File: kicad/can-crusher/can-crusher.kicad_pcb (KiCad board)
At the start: 2 copper layers, 21 parts, among them J1 Stepper Right, J2 Control UART, J3 Ext power, J4 Stepper Left, J5 Barrel_Jack, J6 Expansion Port, Q1 IRF4905, Q2 BS170, SW1 Reboot, SW2 User Interaction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

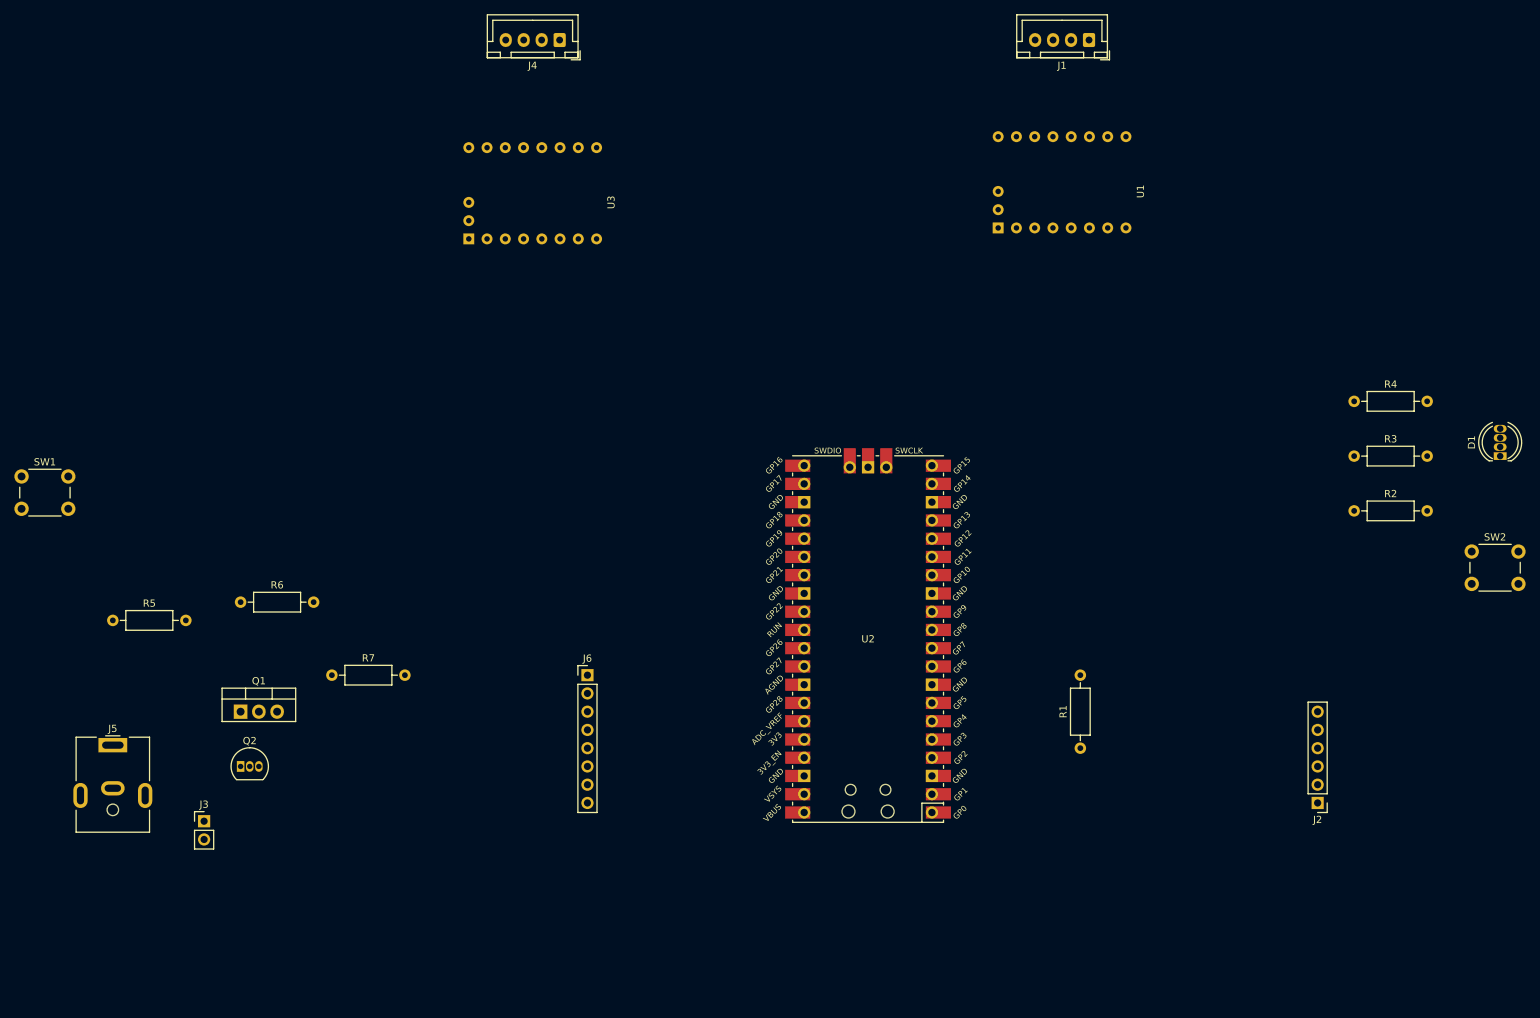
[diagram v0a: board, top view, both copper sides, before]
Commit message: Give better name to project lib storage dir
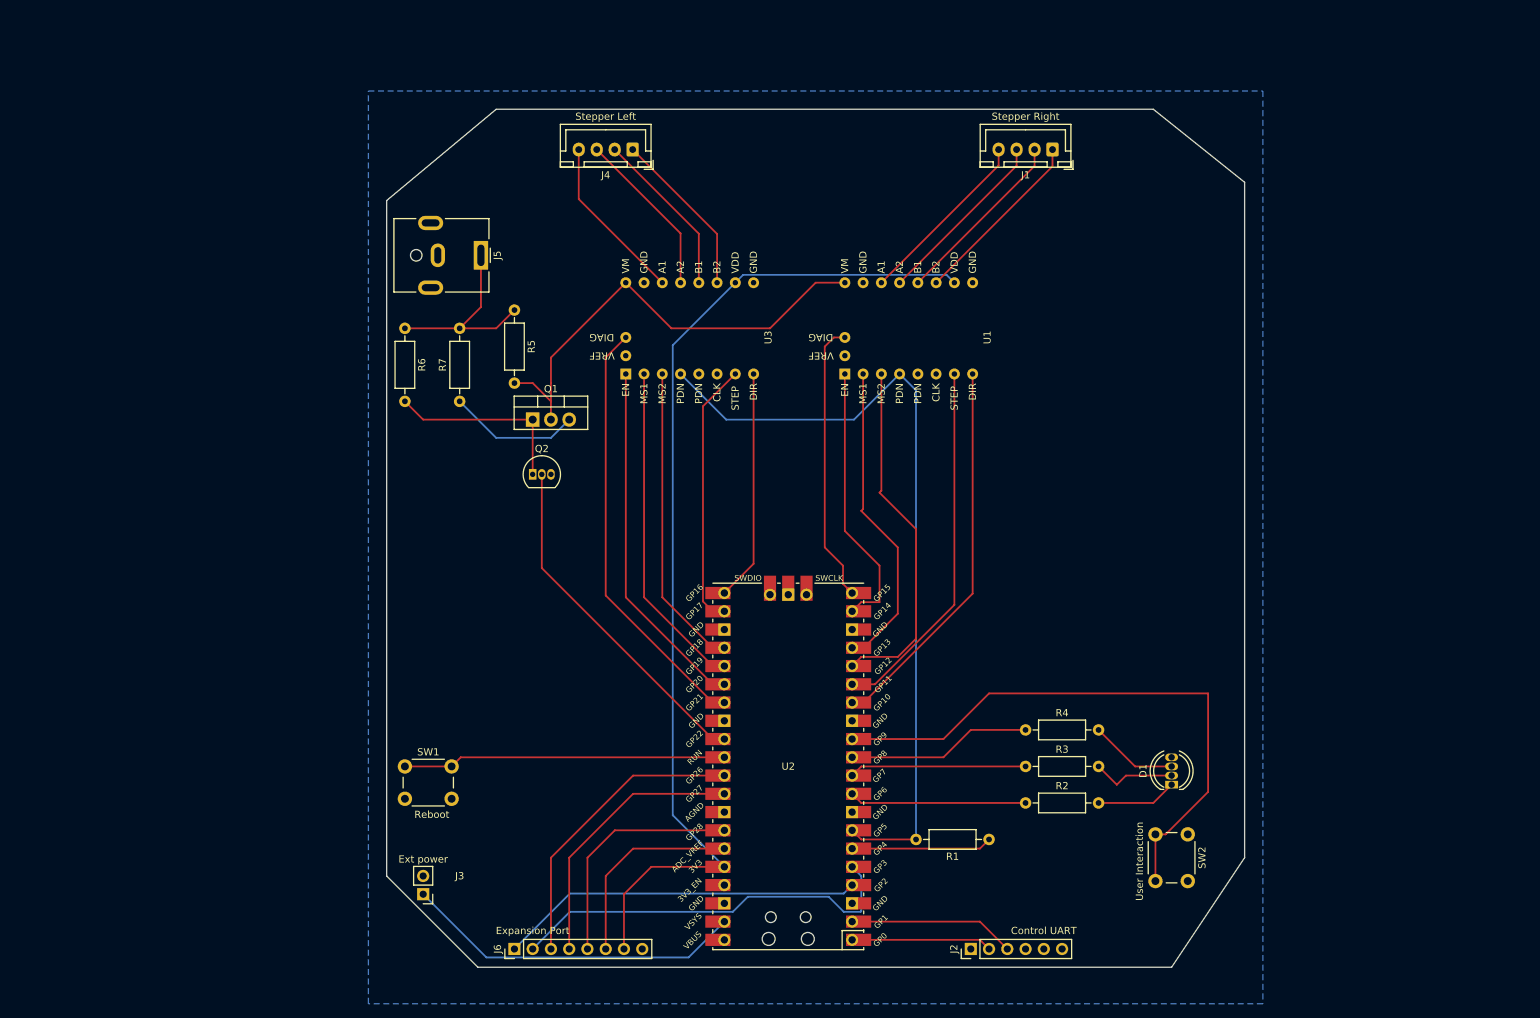
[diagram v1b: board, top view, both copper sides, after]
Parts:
- moved J5 85.3 mm to (104.6, 53.3), turned to -90 degrees
- moved R5 70.6 mm to (109.2, 61.0), turned to -90 degrees
- moved SW1 66.9 mm to (94.0, 124.5)
- moved D1 64.7 mm to (200.7, 127.0)
- moved R4 64.7 mm to (180.3, 119.4)
- moved R3 62.9 mm to (180.3, 124.5)
- moved R2 61.2 mm to (180.3, 129.5)
- moved Q1 57.5 mm to (111.8, 76.2)
- moved Q2 57.5 mm to (111.8, 83.8)
- moved SW2 55.8 mm to (202.9, 133.9), turned to -90 degrees
- moved J2 52.4 mm to (172.7, 149.9), turned to 90 degrees
- moved R6 44.4 mm to (94.0, 63.5), turned to -90 degrees
- moved R7 42.0 mm to (101.6, 73.7), turned to 90 degrees
- moved J6 39.4 mm to (109.2, 149.9), turned to 90 degrees
- moved J3 32.1 mm to (96.5, 142.2), turned to 180 degrees
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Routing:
- net +3.3V: track 0.00 -> 142.4 mm
- net /STEP_TXRX: track 0.00 -> 110.9 mm
- net Net-(SW2-Pad2): track 0.00 -> 82.1 mm
- net /12V_ON: track 0.00 -> 65.2 mm
- net Net-(U2-Pad27): track 0.00 -> 59.7 mm
- net Net-(J6-Pad2): track 0.00 -> 56.3 mm
- net Net-(U1-Pad8): track 0.00 -> 53.6 mm
- net Net-(U1-Pad7): track 0.00 -> 50.9 mm
- net Net-(J6-Pad1): track 0.00 -> 50.7 mm
- net Net-(U2-Pad26): track 0.00 -> 49.8 mm
- net Net-(U1-Pad3): track 0.00 -> 49.5 mm
- net Net-(Q2-Pad2): track 0.00 -> 48.3 mm
- net VCC: track 0.00 -> 47.6 mm
- net Net-(U2-Pad25): track 0.00 -> 46.2 mm
- net Net-(SW1-Pad1): track 0.00 -> 45.0 mm
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- added copper zone on B.Cu, net GND
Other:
- board outline added: 119.4 x 119.4 mm

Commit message: Make board more compact; make power traces appropriate sized.
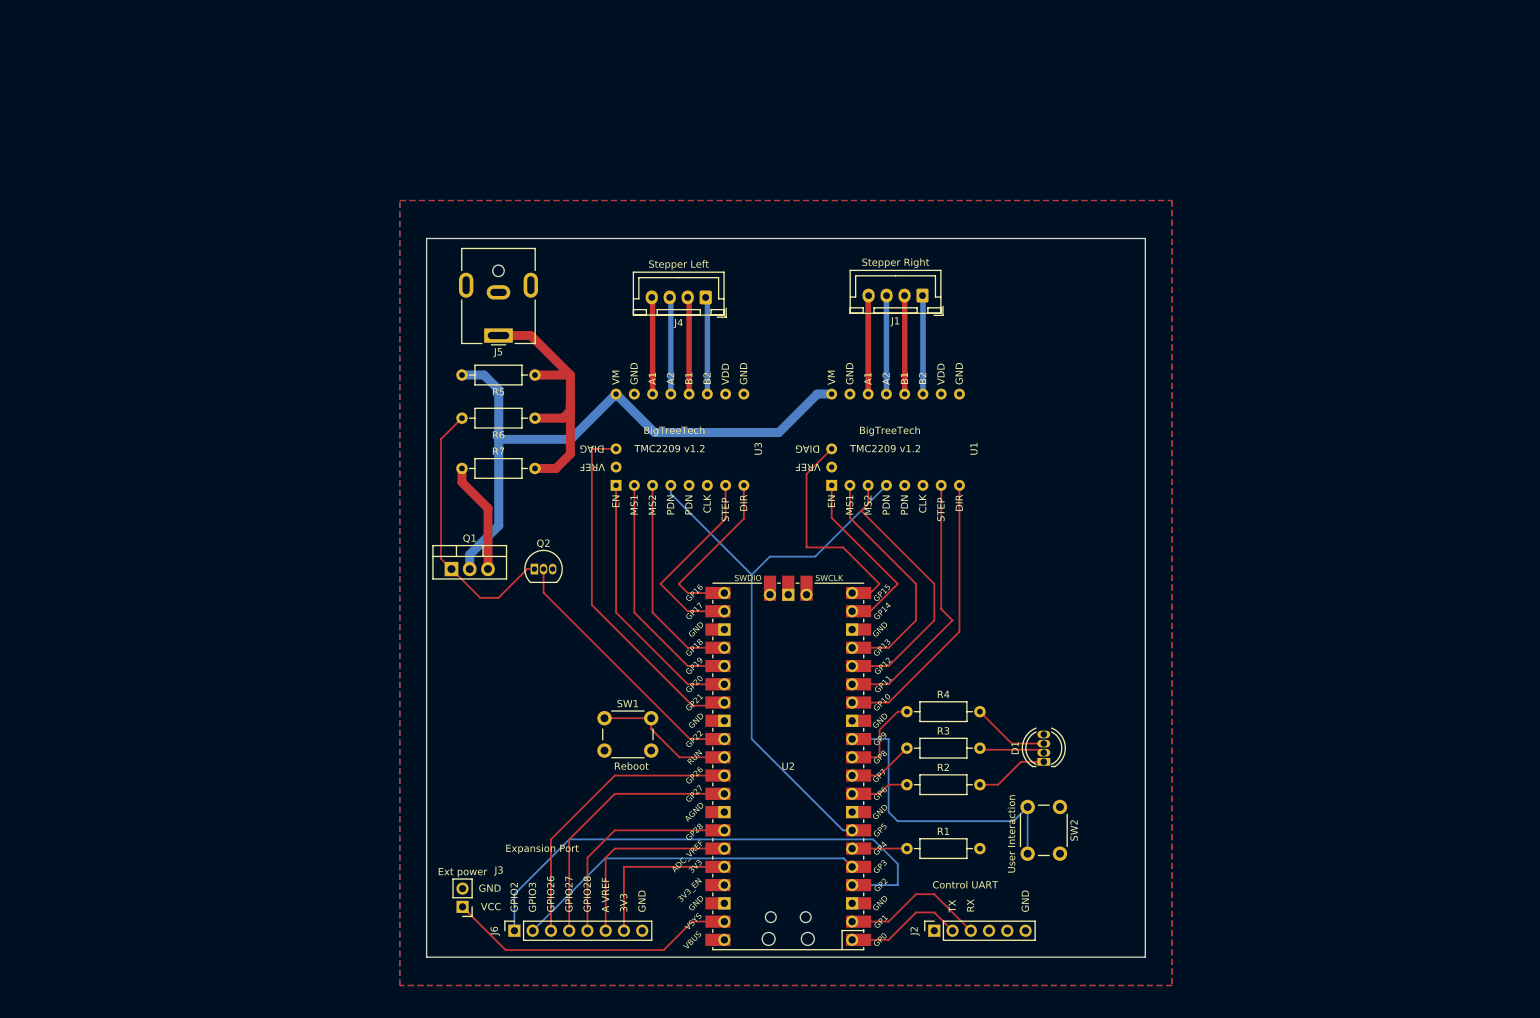
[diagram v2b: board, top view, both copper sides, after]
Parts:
- J2: footprint Connector_PinHeader_2.54mm:PinHeader_1x06_P2.54mm_Vertical -> Connector_PinSocket_2.54mm:PinSocket_1x06_P2.54mm_Vertical
- J6: footprint Connector_PinHeader_2.54mm:PinHeader_1x08_P2.54mm_Vertical -> Connector_PinSocket_2.54mm:PinSocket_1x08_P2.54mm_Vertical
- moved SW1 28.6 mm to (121.8, 117.8)
- moved J1 27.2 mm to (166.0, 58.9)
- moved Q1 23.7 mm to (100.5, 97.0)
- moved J4 22.9 mm to (135.8, 59.2)
- moved R6 22.0 mm to (112.1, 76.0), turned to 180 degrees
- moved SW2 18.2 mm to (185.1, 130.1)
- moved D1 18.1 mm to (182.9, 123.8)
- moved R2 16.7 mm to (163.8, 127.0)
- moved R3 16.7 mm to (163.8, 121.9)
- moved R4 16.7 mm to (163.8, 116.8)
- moved U1 15.6 mm to (173.7, 80.3)
- moved U3 15.6 mm to (143.7, 80.3)
- moved Q2 13.2 mm to (112.0, 97.0)
- moved R1 11.5 mm to (163.8, 135.9), turned to 0 degrees
- moved J5 11.4 mm to (107.0, 64.5), turned to 180 degrees
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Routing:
- net +3.3V: track 142.4 -> 22.9 mm
- net Net-(SW2-Pad2): track 82.1 -> 42.4 mm
- net /STEP_TXRX: track 110.9 -> 83.1 mm
- net Net-(SW1-Pad1): track 45.0 -> 19.8 mm
- net Net-(J6-Pad1): track 50.7 -> 72.3 mm
- net /12V_ON: track 65.2 -> 86.0 mm
- net Net-(R2-Pad1): track 24.7 -> 8.15 mm
- net Net-(R3-Pad1): track 24.7 -> 9.20 mm
- net Net-(U1-Pad8): track 53.6 -> 39.4 mm
- net Net-(U1-Pad7): track 50.9 -> 37.1 mm
- net Net-(R4-Pad1): track 25.7 -> 12.5 mm
- net Net-(U2-Pad26): track 49.8 -> 36.9 mm
- net Net-(U2-Pad25): track 46.2 -> 33.3 mm
- net Net-(U2-Pad24): track 42.6 -> 29.7 mm
- net Net-(U1-Pad1): track 38.1 -> 25.4 mm
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- added copper zone on F.Cu, net GND
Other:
- board size 119.4 x 119.4 mm -> 100 x 100 mm

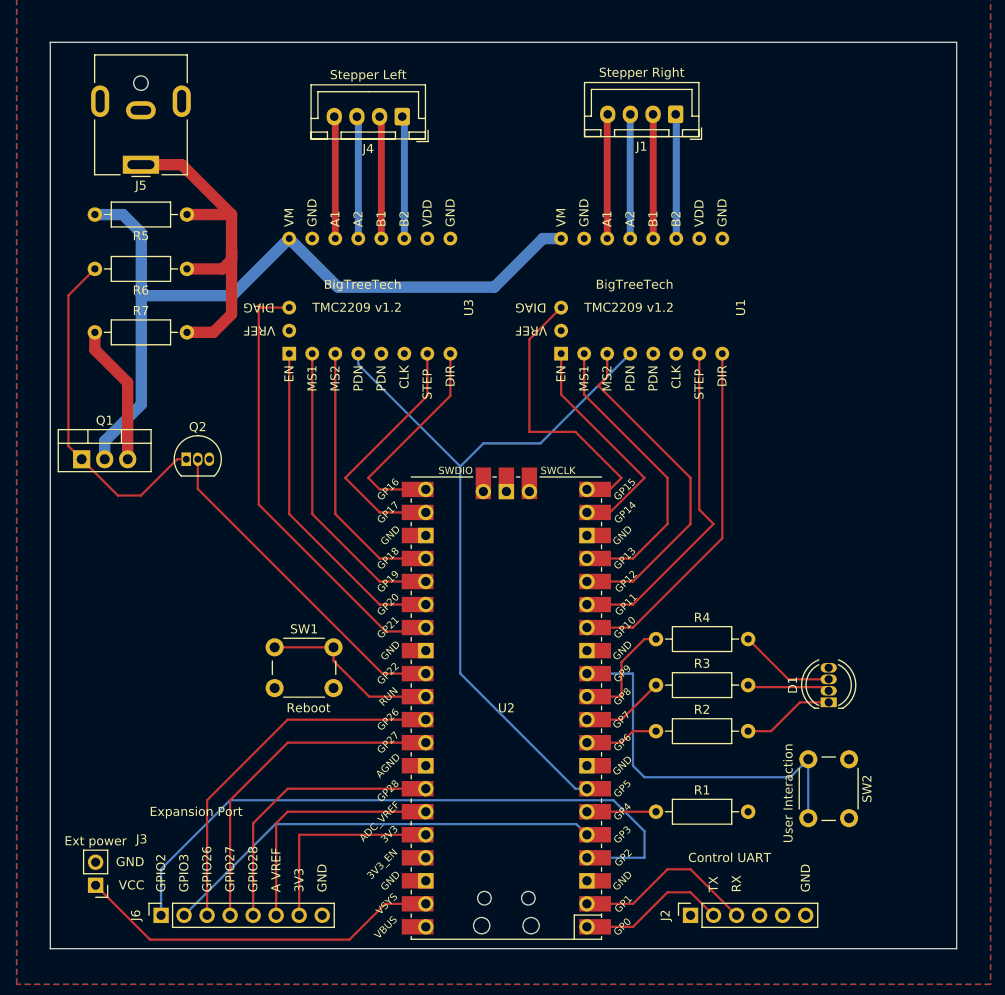
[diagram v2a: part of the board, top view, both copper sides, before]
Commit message: Final REV 1 control board submitted for PCB manufacturing
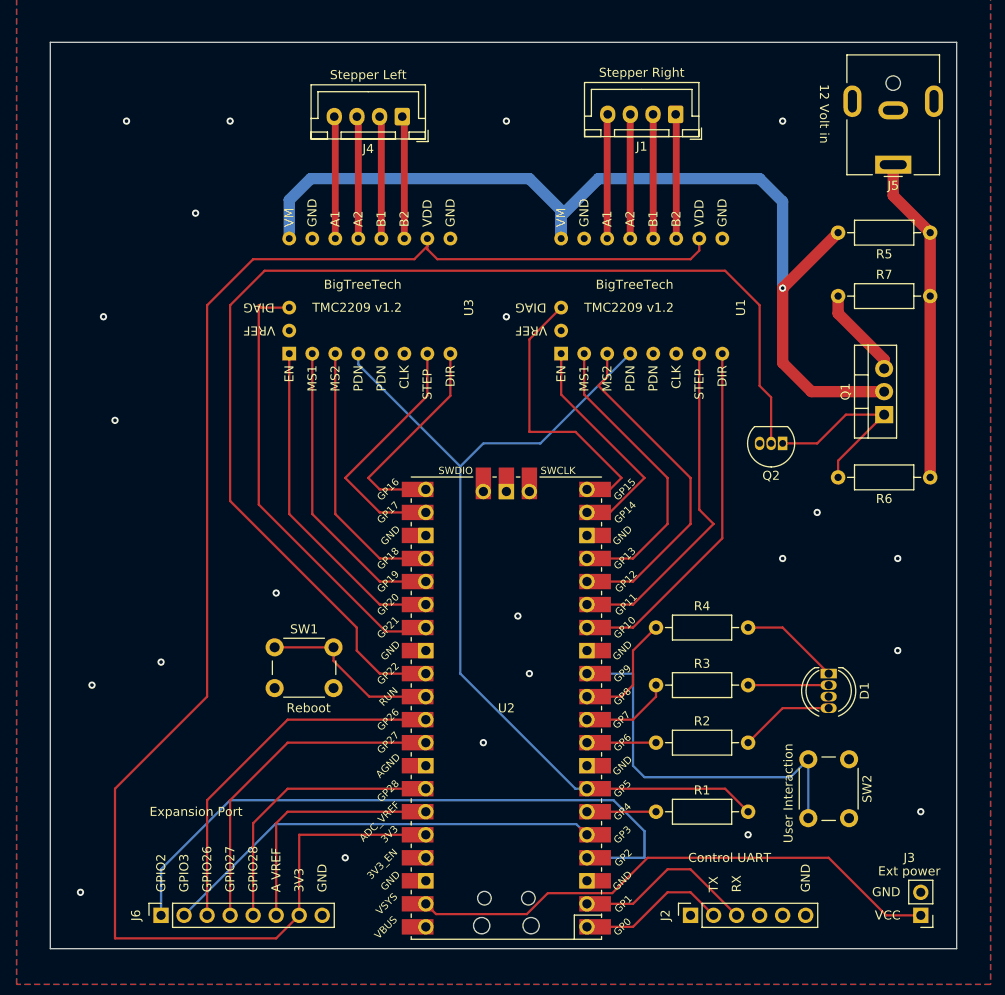
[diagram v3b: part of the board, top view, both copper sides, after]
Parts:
- D1: value LED_RGBK -> LED_BRKG
- Q1: value IRF4905 -> IRF9540N
- R2, R3, R4: value R -> 220
- moved J3 91.1 mm to (193.0, 147.3)
- moved Q1 88.7 mm to (189.0, 92.1), turned to 90 degrees
- moved R6 85.2 mm to (194.1, 99.0)
- moved J5 83.0 mm to (190.0, 64.5)
- moved R7 82.1 mm to (183.9, 79.0)
- moved R5 82.0 mm to (194.1, 72.0)
- moved Q2 65.8 mm to (177.8, 95.2), turned to 180 degrees
- moved D1 3.17 mm to (182.9, 120.7), turned to -90 degrees
- moved R2 1.27 mm to (163.8, 128.3)
- moved R4 1.27 mm to (163.8, 115.6)
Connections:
- D1 pad 3: Net-(D1-Pad3) -> GND
- D1 pad 4: GND -> Net-(D1-Pad4)
- R2 pad 2: Net-(D1-Pad1) -> Net-(D1-Pad4)
- R4 pad 2: Net-(D1-Pad3) -> Net-(D1-Pad1)
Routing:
- net +3.3V: track 22.9 -> 179.5 mm
- net Net-(Q2-Pad2): track 36.9 -> 129.9 mm
- net /12V_ON: track 86.0 -> 108.4 mm, vias 0 -> 1
- net VCC: track 40.6 -> 60.3 mm
- net /STEP_TXRX: track 83.1 -> 101.9 mm
- net Net-(Q1-Pad1): track 37.7 -> 21.5 mm
- net Net-(D1-Pad3): track 10.7 -> 0.00 mm
- net Net-(D1-Pad4): track 0.00 -> 10.5 mm
- net Net-(Q1-Pad3): track 15.5 -> 10.1 mm
- net +12V: track 40.3 -> 36.2 mm
- net Net-(D1-Pad1): track 10.2 -> 11.0 mm
- net Net-(R3-Pad1): track 9.20 -> 9.94 mm
- net Net-(R2-Pad1): track 8.15 -> 7.62 mm
- net Net-(R4-Pad1): track 12.5 -> 13.0 mm
- net GND: vias 0 -> 22
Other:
- board text added: "${COMPANY}"
- board text added: "${ISSUE_DATE} - Rev ${REVISION}"
- board text added: "${TITLE}"
- board text added: "JLCJLCJLCJLC"
